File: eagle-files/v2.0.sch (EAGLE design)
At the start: 37 parts, among them U2 MLX90614_

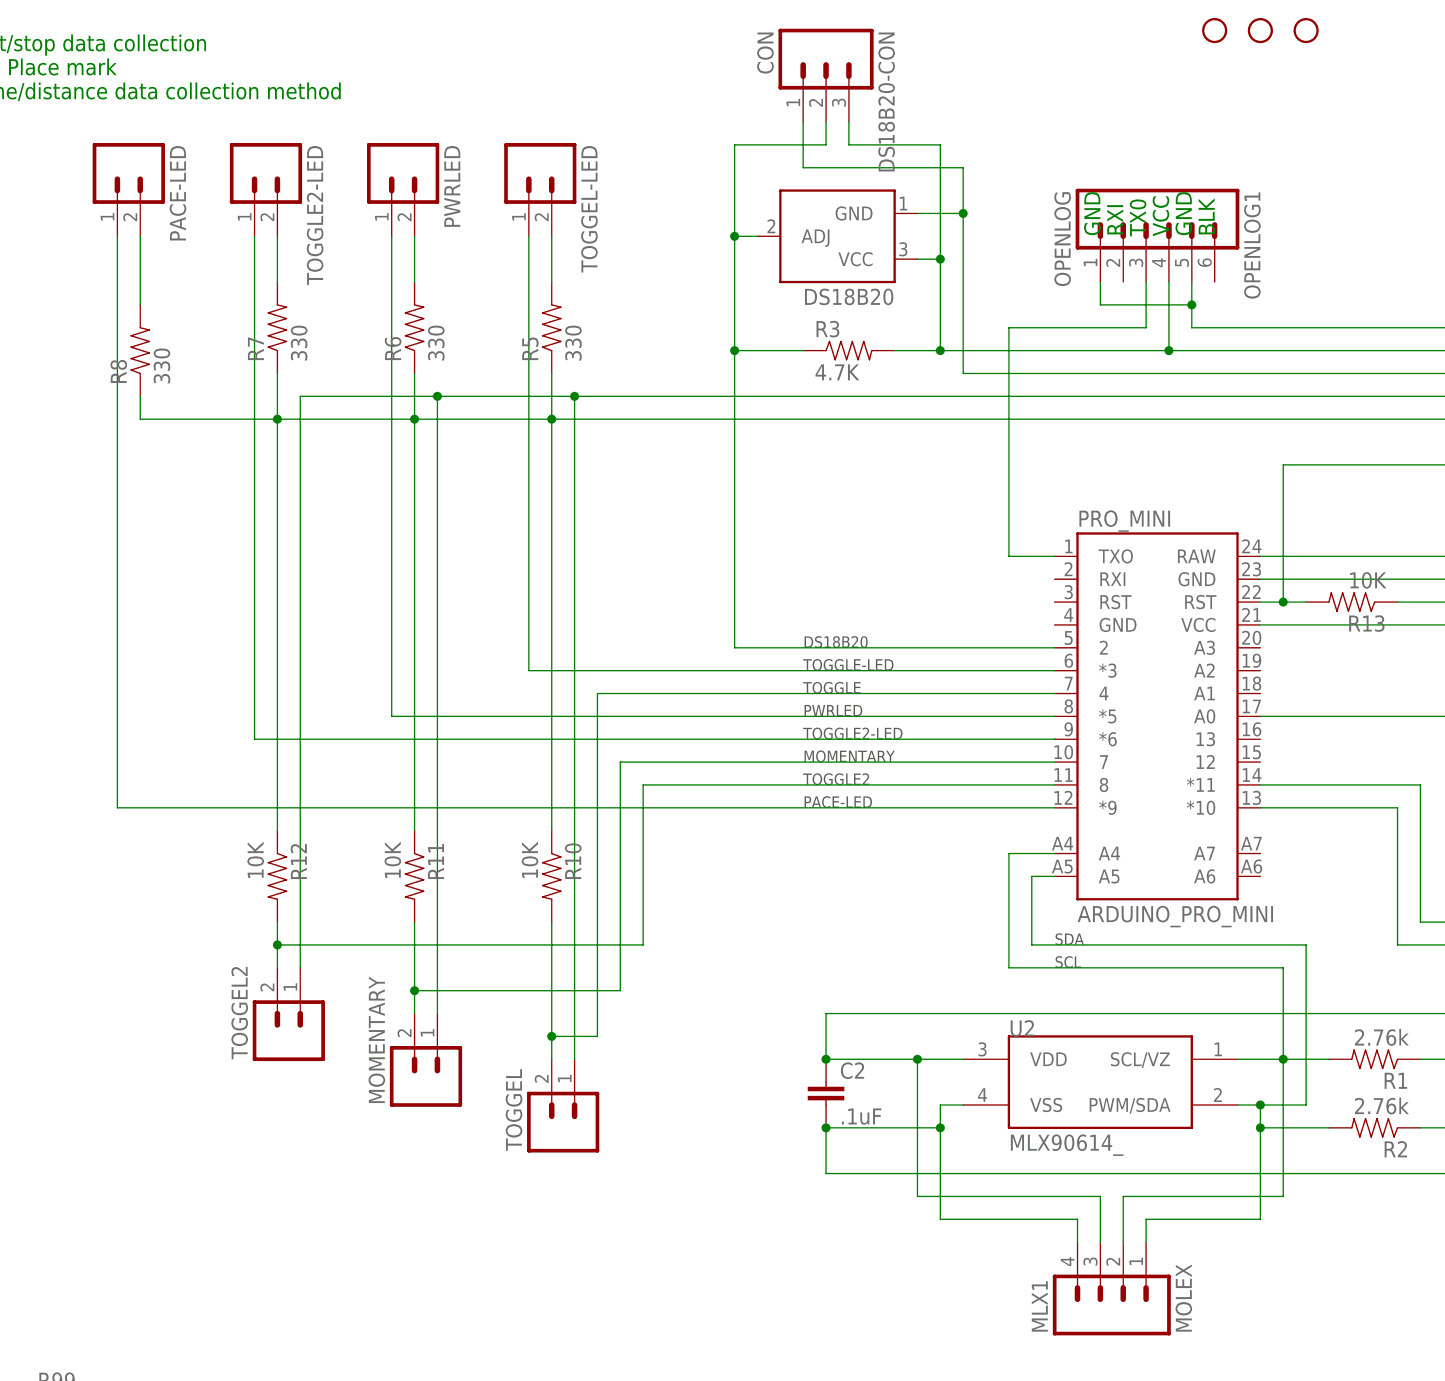
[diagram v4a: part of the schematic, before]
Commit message: added base code for Arduino
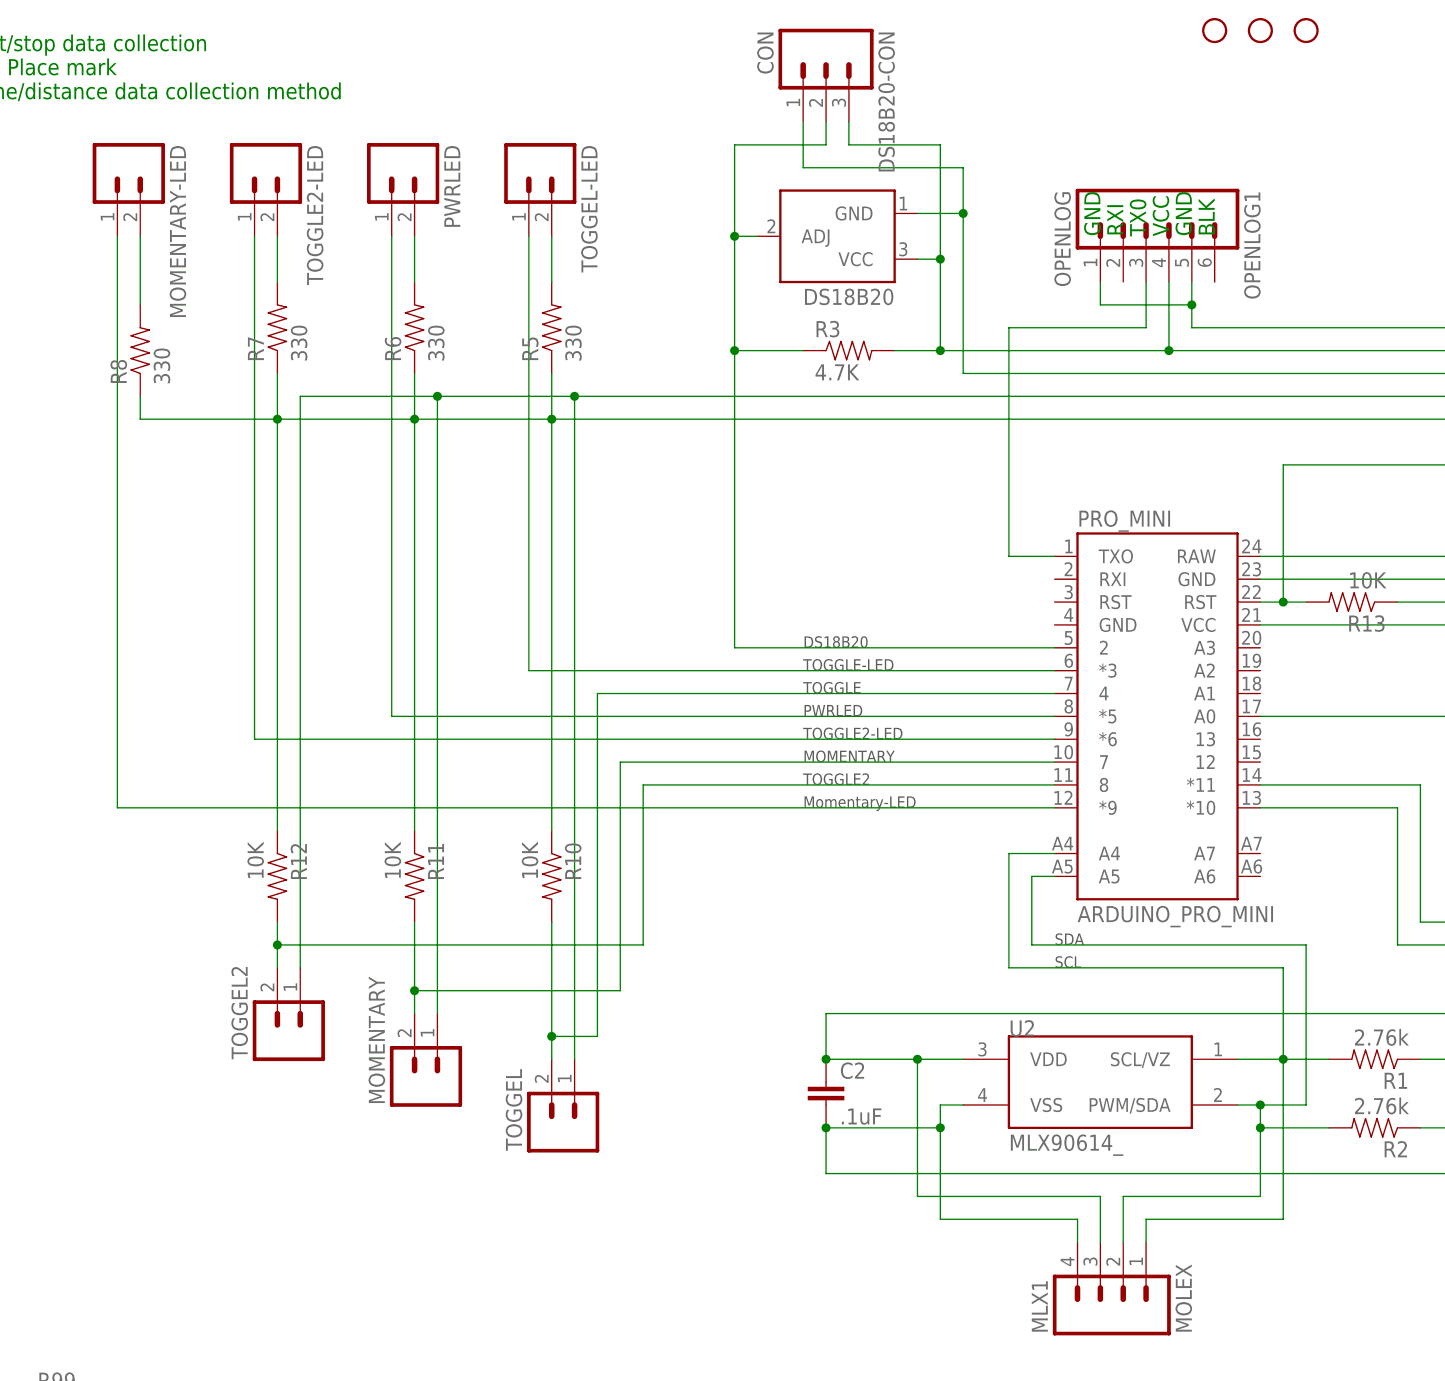
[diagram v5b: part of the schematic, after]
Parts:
- renumbered PACE-LED to MOMENTARY-LED
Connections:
- removed net N$7: MLX1.1, PRO_MINI.A5, R2.2, U2.PWM/SDA
- removed net N$9: MLX1.2, PRO_MINI.A4, R1.2, U2.SCL/VZ
- new net N$21: MLX1.2, PRO_MINI.A5, R2.2, U2.PWM/SDA
- new net N$22: MLX1.1, PRO_MINI.A4, R1.2, U2.SCL/VZ
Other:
- note added: "Momentary-LED"
- note removed: "PACE-LED"
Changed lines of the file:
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@@
 <part name="WHL-PWR" library="SparkFun-Connectors" deviceset="M02" device="3.5MM_LOCK" value=""/>
 <part name="WHL-DATA" library="SparkFun-Connectors" deviceset="M02" device="3.5MM_LOCK" value=""/>
-<part name="PACE-LED" library="SparkFun-Connectors" deviceset="M02" device="3.5MM_LOCK" value=""/>
+<part name="MOMENTARY-LED" library="SparkFun-Connectors" deviceset="M02" device="3.5MM_LOCK" value=""/>
 <part name="R8" library="SparkFun-Resistors" deviceset="330OHM1/10W1%(0603)" device="" value="330"/>
 <part name="DS18B20-CON" library="SparkFun-Connectors" deviceset="M03" device="SCREW_LOCK" value="CON"/>
@@
 <text x="106.68" y="99.06" size="1.27" layer="97">TOGGLE2</text>
 <text x="106.68" y="101.6" size="1.27" layer="97">MOMENTARY</text>
-<text x="106.68" y="96.52" size="1.27" layer="97">PACE-LED</text>
+<text x="106.68" y="96.52" size="1.27" layer="97">Momentary-LED</text>
 <text x="106.68" y="104.14" size="1.27" layer="97">TOGGLE2-LED</text>
 <text x="106.68" y="106.68" size="1.27" layer="97">PWRLED</text>
@@
 <instance part="WHL-PWR" gate="G$1" x="195.58" y="96.52" rot="R180"/>
 <instance part="WHL-DATA" gate="G$1" x="195.58" y="83.82" rot="R180"/>
-<instance part="PACE-LED" gate="G$1" x="30.48" y="167.64" rot="R270"/>
+<instance part="MOMENTARY-LED" gate="G$1" x="30.48" y="167.64" rot="R270"/>
 <instance part="R8" gate="G$1" x="33.02" y="147.32" rot="R90"/>
 <instance part="DS18B20-CON" gate="G$1" x="109.22" y="180.34" rot="R270"/>
@@
 </segment>
 </net>
-<net name="N$7" class="0">
-<segment>
-<pinref part="MLX1" gate="G$1" pin="1"/>
-<wire x1="144.78" y1="48.26" x2="144.78" y2="50.8" width="0.1524" layer="91"/>
-<wire x1="144.78" y1="50.8" x2="157.48" y2="50.8" width="0.1524" layer="91"/>
-<pinref part="U2" gate="G$1" pin="PWM/SDA"/>
-<wire x1="157.48" y1="50.8" x2="157.48" y2="60.96" width="0.1524" layer="91"/>
-<wire x1="157.48" y1="60.96" x2="157.48" y2="63.5" width="0.1524" layer="91"/>
-<wire x1="157.48" y1="63.5" x2="154.94" y2="63.5" width="0.1524" layer="91"/>
-<wire x1="157.48" y1="63.5" x2="162.56" y2="63.5" width="0.1524" layer="91"/>
-<wire x1="162.56" y1="63.5" x2="162.56" y2="81.28" width="0.1524" layer="91"/>
-<wire x1="162.56" y1="81.28" x2="132.08" y2="81.28" width="0.1524" layer="91"/>
-<pinref part="PRO_MINI" gate="G$1" pin="A5"/>
-<wire x1="132.08" y1="81.28" x2="132.08" y2="88.9" width="0.1524" layer="91"/>
-<wire x1="132.08" y1="88.9" x2="134.62" y2="88.9" width="0.1524" layer="91"/>
-<junction x="157.48" y="63.5"/>
-<pinref part="R2" gate="G$1" pin="2"/>
-<wire x1="165.1" y1="60.96" x2="157.48" y2="60.96" width="0.1524" layer="91"/>
-<junction x="157.48" y="60.96"/>
-</segment>
-</net>
-<net name="N$9" class="0">
-<segment>
-<pinref part="MLX1" gate="G$1" pin="2"/>
-<wire x1="142.24" y1="48.26" x2="142.24" y2="53.34" width="0.1524" layer="91"/>
-<wire x1="142.24" y1="53.34" x2="160.02" y2="53.34" width="0.1524" layer="91"/>
-<pinref part="U2" gate="G$1" pin="SCL/VZ"/>
-<wire x1="160.02" y1="53.34" x2="160.02" y2="68.58" width="0.1524" layer="91"/>
-<wire x1="160.02" y1="68.58" x2="154.94" y2="68.58" width="0.1524" layer="91"/>
-<wire x1="160.02" y1="68.58" x2="160.02" y2="78.74" width="0.1524" layer="91"/>
-<wire x1="160.02" y1="78.74" x2="129.54" y2="78.74" width="0.1524" layer="91"/>
-<pinref part="PRO_MINI" gate="G$1" pin="A4"/>
-<wire x1="129.54" y1="78.74" x2="129.54" y2="91.44" width="0.1524" layer="91"/>
-<wire x1="129.54" y1="91.44" x2="134.62" y2="91.44" width="0.1524" layer="91"/>
-<junction x="160.02" y="68.58"/>
-<pinref part="R1" gate="G$1" pin="2"/>
-<wire x1="165.1" y1="68.58" x2="160.02" y2="68.58" width="0.1524" layer="91"/>
-</segment>
-</net>
 <net name="5V" class="1">
 <segment>
@@
 <net name="N$16" class="0">
 <segment>
-<pinref part="PACE-LED" gate="G$1" pin="2"/>
+<pinref part="MOMENTARY-LED" gate="G$1" pin="2"/>
 <pinref part="R8" gate="G$1" pin="2"/>
 <wire x1="33.02" y1="152.4" x2="33.02" y2="160.02" width="0.1524" layer="91"/>
@@
 <net name="N$17" class="0">
 <segment>
-<pinref part="PACE-LED" gate="G$1" pin="1"/>
+<pinref part="MOMENTARY-LED" gate="G$1" pin="1"/>
 <pinref part="PRO_MINI" gate="G$1" pin="*9"/>
 <wire x1="30.48" y1="160.02" x2="30.48" y2="96.52" width="0.1524" layer="91"/>
@@
 </segment>
 </net>
+<net name="N$21" class="0">
+<segment>
+<pinref part="MLX1" gate="G$1" pin="2"/>
+<wire x1="142.24" y1="48.26" x2="142.24" y2="53.34" width="0.1524" layer="91"/>
+<pinref part="U2" gate="G$1" pin="PWM/SDA"/>
+<wire x1="157.48" y1="60.96" x2="157.48" y2="63.5" width="0.1524" layer="91"/>
+<wire x1="157.48" y1="63.5" x2="154.94" y2="63.5" width="0.1524" layer="91"/>
+<wire x1="157.48" y1="63.5" x2="162.56" y2="63.5" width="0.1524" layer="91"/>
+<wire x1="162.56" y1="63.5" x2="162.56" y2="81.28" width="0.1524" layer="91"/>
+<wire x1="162.56" y1="81.28" x2="132.08" y2="81.28" width="0.1524" layer="91"/>
+<pinref part="PRO_MINI" gate="G$1" pin="A5"/>
+<wire x1="132.08" y1="81.28" x2="132.08" y2="88.9" width="0.1524" layer="91"/>
+<wire x1="132.08" y1="88.9" x2="134.62" y2="88.9" width="0.1524" layer="91"/>
+<junction x="157.48" y="63.5"/>
+<pinref part="R2" gate="G$1" pin="2"/>
+<wire x1="165.1" y1="60.96" x2="157.48" y2="60.96" width="0.1524" layer="91"/>
+<wire x1="142.24" y1="53.34" x2="157.48" y2="53.34" width="0.1524" layer="91"/>
+<wire x1="157.48" y1="53.34" x2="157.48" y2="60.96" width="0.1524" layer="91"/>
+<junction x="157.48" y="60.96"/>
+</segment>
+</net>
+<net name="N$22" class="0">
+<segment>
+<wire x1="144.78" y1="50.8" x2="160.02" y2="50.8" width="0.1524" layer="91"/>
+<pinref part="MLX1" gate="G$1" pin="1"/>
+<wire x1="144.78" y1="48.26" x2="144.78" y2="50.8" width="0.1524" layer="91"/>
+<pinref part="U2" gate="G$1" pin="SCL/VZ"/>
+<wire x1="160.02" y1="68.58" x2="154.94" y2="68.58" width="0.1524" layer="91"/>
+<wire x1="160.02" y1="68.58" x2="160.02" y2="78.74" width="0.1524" layer="91"/>
+<wire x1="160.02" y1="78.74" x2="129.54" y2="78.74" width="0.1524" layer="91"/>
+<pinref part="PRO_MINI" gate="G$1" pin="A4"/>
+<wire x1="129.54" y1="78.74" x2="129.54" y2="91.44" width="0.1524" layer="91"/>
+<wire x1="129.54" y1="91.44" x2="134.62" y2="91.44" width="0.1524" layer="91"/>
+<junction x="160.02" y="68.58"/>
+<pinref part="R1" gate="G$1" pin="2"/>
+<wire x1="165.1" y1="68.58" x2="160.02" y2="68.58" width="0.1524" layer="91"/>
+<wire x1="160.02" y1="50.8" x2="160.02" y2="68.58" width="0.1524" layer="91"/>
+</segment>
+</net>

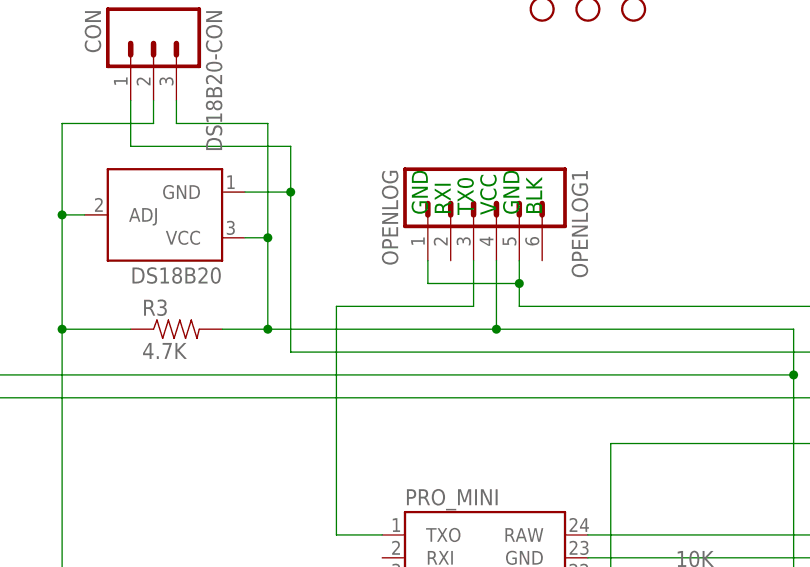
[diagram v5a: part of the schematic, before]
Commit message: updated txo rxi for eagle
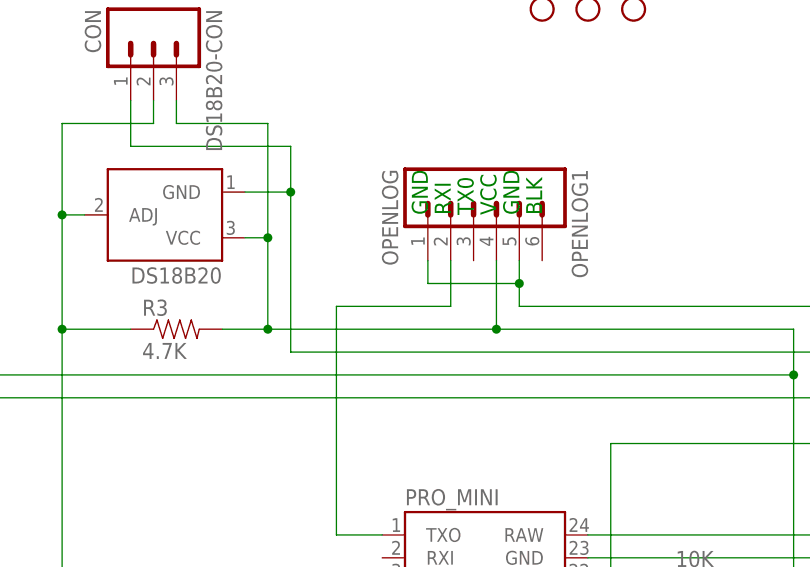
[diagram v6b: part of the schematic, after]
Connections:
- net N$8: now also OPENLOG1.2; no longer OPENLOG1.3
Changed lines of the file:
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@@
 <net name="N$8" class="0">
 <segment>
-<pinref part="OPENLOG1" gate="G$1" pin="3"/>
-<wire x1="144.78" y1="154.94" x2="144.78" y2="149.86" width="0.1524" layer="91"/>
-<wire x1="144.78" y1="149.86" x2="129.54" y2="149.86" width="0.1524" layer="91"/>
 <pinref part="PRO_MINI" gate="G$1" pin="TXO"/>
 <wire x1="129.54" y1="149.86" x2="129.54" y2="124.46" width="0.1524" layer="91"/>
 <wire x1="129.54" y1="124.46" x2="134.62" y2="124.46" width="0.1524" layer="91"/>
+<pinref part="OPENLOG1" gate="G$1" pin="2"/>
+<wire x1="129.54" y1="149.86" x2="142.24" y2="149.86" width="0.1524" layer="91"/>
+<wire x1="142.24" y1="149.86" x2="142.24" y2="154.94" width="0.1524" layer="91"/>
 </segment>
 </net>

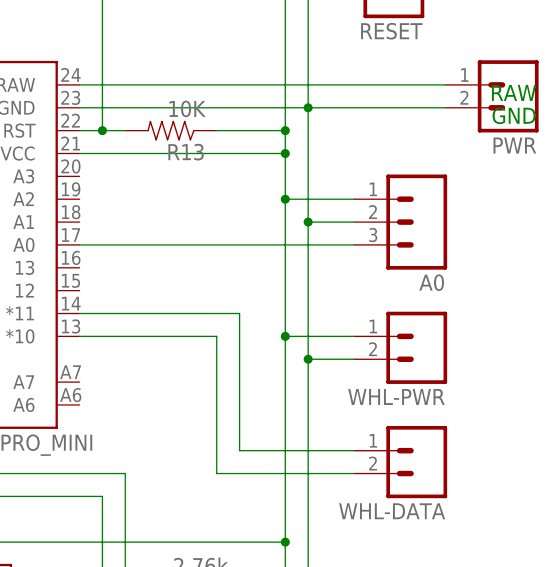
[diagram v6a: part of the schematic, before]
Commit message: updated and named my analog to tmp36
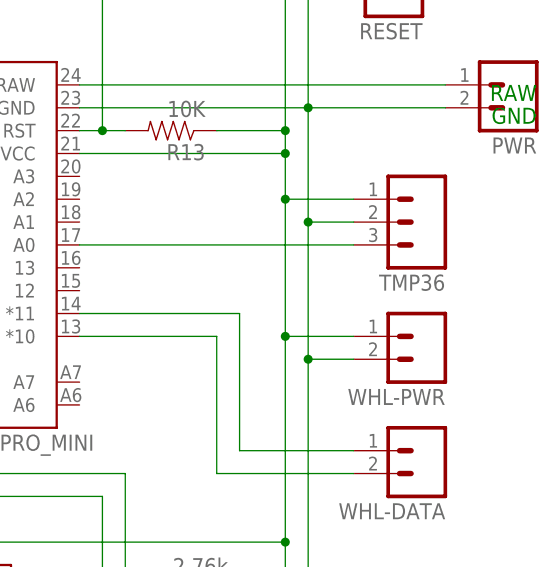
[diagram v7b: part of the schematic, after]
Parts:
- renumbered A0 to TMP36
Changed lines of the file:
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@@
 <part name="RESET" library="SparkFun-Connectors" deviceset="M02" device="3.5MM_LOCK" value=""/>
 <part name="R13" library="SparkFun-Resistors" deviceset="10KOHM1/10W1%(0603)" device="0603" value="10K"/>
-<part name="A0" library="SparkFun-Connectors" deviceset="M03" device="SCREW_LOCK"/>
+<part name="TMP36" library="SparkFun-Connectors" deviceset="M03" device="SCREW_LOCK"/>
 </parts>
 <sheets>
@@
 <instance part="RESET" gate="G$1" x="193.04" y="137.16" rot="R180"/>
 <instance part="R13" gate="G$1" x="167.64" y="119.38" rot="R180"/>
-<instance part="A0" gate="G$1" x="195.58" y="109.22" rot="R180"/>
+<instance part="TMP36" gate="G$1" x="195.58" y="109.22" rot="R180"/>
 </instances>
 <busses>
@@
 <wire x1="185.42" y1="137.16" x2="182.88" y2="137.16" width="0.1524" layer="91"/>
 <junction x="182.88" y="137.16"/>
-<pinref part="A0" gate="G$1" pin="2"/>
+<pinref part="TMP36" gate="G$1" pin="2"/>
 <wire x1="187.96" y1="109.22" x2="182.88" y2="109.22" width="0.1524" layer="91"/>
 <junction x="182.88" y="109.22"/>
@@
 <wire x1="172.72" y1="119.38" x2="180.34" y2="119.38" width="0.1524" layer="91"/>
 <junction x="180.34" y="119.38"/>
-<pinref part="A0" gate="G$1" pin="1"/>
+<pinref part="TMP36" gate="G$1" pin="1"/>
 <wire x1="187.96" y1="111.76" x2="180.34" y2="111.76" width="0.1524" layer="91"/>
 <junction x="180.34" y="111.76"/>
@@
 <net name="N$20" class="0">
 <segment>
-<pinref part="A0" gate="G$1" pin="3"/>
+<pinref part="TMP36" gate="G$1" pin="3"/>
 <pinref part="PRO_MINI" gate="G$1" pin="A0"/>
 <wire x1="187.96" y1="106.68" x2="157.48" y2="106.68" width="0.1524" layer="91"/>
